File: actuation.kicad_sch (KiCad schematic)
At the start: 16 parts, among them J1 ACTUATION, U1 PCA9615

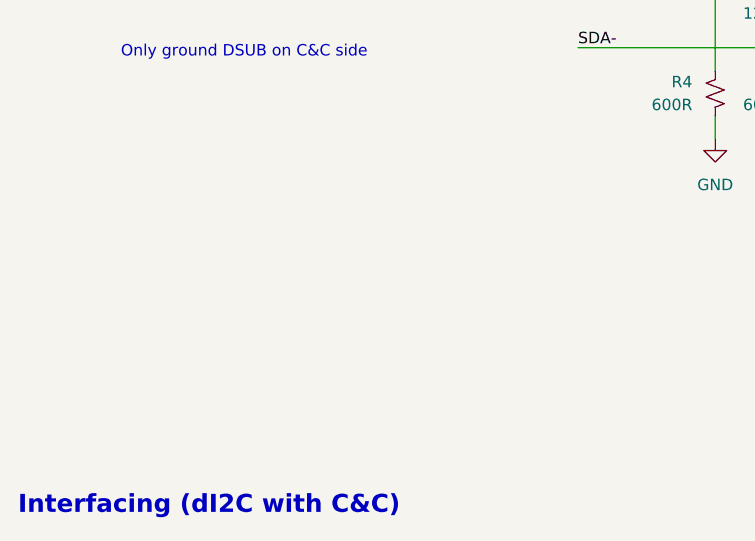
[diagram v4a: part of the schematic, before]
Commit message: TVS diodes for ESD protection on inputs
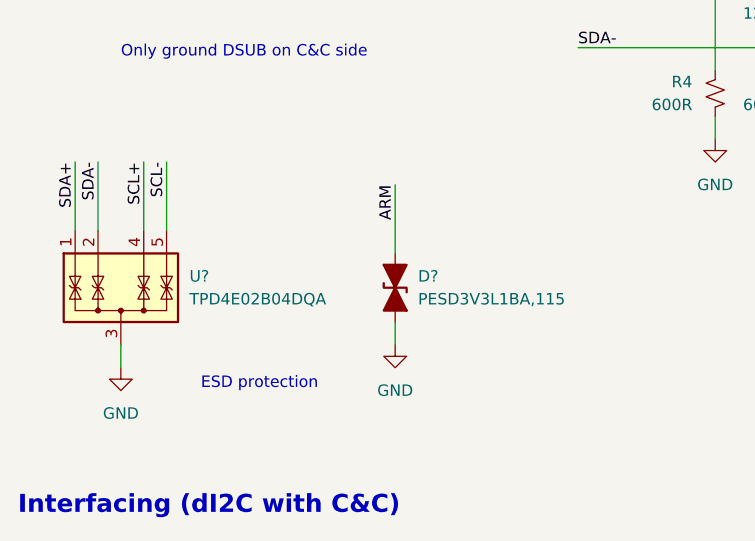
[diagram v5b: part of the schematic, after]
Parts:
- added D?: PESD3V3L1BA,115, Diode_SMD:D_SOD-323, symbol Device:D_TVS_Filled
- added U?: TPD4E02B04DQA, Package_SON:USON-10_2.5x1.0mm_P0.5mm, symbol Power_Protection:TPD4E02B04DQA
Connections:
- net ARM: now also D?.2 (A2)
- net GND: now also D?.1 (A1), U?.3 (G), U?.8 (G)
- net SCL+: now also U?.4 (IO3)
- net SCL-: now also U?.5 (IO4)
- net SDA+: now also U?.1 (IO1)
- net SDA-: now also U?.2 (IO2)
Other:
- note added: "ESD protection"
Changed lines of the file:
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@@
+    (stroke (width 0) (type default) (color 0 0 0 0))
+  )
+  (wire (pts (xy 58.42 96.52) (xy 58.42 104.14))
     (stroke (width 0) (type default) (color 0 0 0 0))
   )
@@
     (stroke (width 0) (type default) (color 0 0 0 0))
   )
+  (wire (pts (xy 25.4 93.98) (xy 25.4 101.6))
+    (stroke (width 0) (type default) (color 0 0 0 0))
+  )
   (wire (pts (xy 143.51 41.91) (xy 143.51 39.37))
     (stroke (width 0) (type default) (color 0 0 0 0))
@@
     (stroke (width 0) (type default) (color 0 0 0 0))
   )
+  (wire (pts (xy 58.42 111.76) (xy 58.42 114.3))
+    (stroke (width 0) (type default) (color 0 0 0 0))
+  )
   (wire (pts (xy 40.64 52.07) (xy 33.02 52.07))
     (stroke (width 0) (type default) (color 0 0 0 0))
@@
     (stroke (width 0) (type default) (color 0 0 0 0))
   )
+  (wire (pts (xy 22.86 93.98) (xy 22.86 101.6))
+    (stroke (width 0) (type default) (color 0 0 0 0))
+  )
   (wire (pts (xy 218.44 81.28) (xy 224.79 81.28))
     (stroke (width 0) (type default) (color 0 0 0 0))
@@
     (stroke (width 0) (type default) (color 0 0 0 0))
   )
+  (wire (pts (xy 30.48 93.98) (xy 30.48 101.6))
+    (stroke (width 0) (type default) (color 0 0 0 0))
+  )
   (wire (pts (xy 143.51 29.21) (xy 143.51 31.75))
     (stroke (width 0) (type default) (color 0 0 0 0))
@@
     (stroke (width 0) (type default) (color 0 0 0 0))
   )
+  (wire (pts (xy 27.94 114.3) (xy 27.94 116.84))
+    (stroke (width 0) (type default) (color 0 0 0 0))
+  )
   (wire (pts (xy 114.3 57.15) (xy 114.3 54.61))
     (stroke (width 0) (type default) (color 0 0 0 0))
@@
   )
   (wire (pts (xy 35.56 44.45) (xy 43.18 44.45))
+    (stroke (width 0) (type default) (color 0 0 0 0))
+  )
+  (wire (pts (xy 33.02 93.98) (xy 33.02 101.6))
     (stroke (width 0) (type default) (color 0 0 0 0))
   )
@@
     (effects (font (size 1.27 1.27)) (justify left bottom))
   )
+  (text "ESD protection" (at 36.83 119.38 0)
+    (effects (font (size 1.27 1.27)) (justify left bottom))
+  )
   (text "~33mA 3.3V consumption" (at 222.25 44.45 0)
     (effects (font (size 1.27 1.27)) (justify left bottom))
@@
     (effects (font (size 1.27 1.27)) (justify left bottom))
   )
+  (label "SCL+" (at 30.48 93.98 270)
+    (effects (font (size 1.27 1.27)) (justify right bottom))
+  )
+  (label "SDA+" (at 22.86 93.98 270)
+    (effects (font (size 1.27 1.27)) (justify right bottom))
+  )
+  (label "ARM" (at 58.42 96.52 270)
+    (effects (font (size 1.27 1.27)) (justify right bottom))
+  )
   (label "SCL-" (at 78.74 66.04 0)
     (effects (font (size 1.27 1.27)) (justify left bottom))
@@
   (label "SDA-" (at 35.56 46.99 0)
     (effects (font (size 1.27 1.27)) (justify left bottom))
+  )
+  (label "SDA-" (at 25.4 93.98 270)
+    (effects (font (size 1.27 1.27)) (justify right bottom))
+  )
+  (label "SCL-" (at 33.02 93.98 270)
+    (effects (font (size 1.27 1.27)) (justify right bottom))
   )
   (label "SDA" (at 168.91 69.85 180)
@@
     )
     (property "Datasheet" "" (id 3) (at 33.02 69.85 0)
+      (effects (font (size 1.27 1.27)) hide)
+    )
+    (pin "1")
+  )
+  (symbol (lib_name "GND_1") (lib_id "power:GND") (at 58.42 114.3 0) (unit 1)
+    (in_bom yes) (on_board yes) (fields_autoplaced)
+    (property "Reference" "#PWR?" (id 0) (at 58.42 120.65 0)
+      (effects (font (size 1.27 1.27)) hide)
+    )
+    (property "Value" "GND" (id 1) (at 58.42 119.38 0))
+    (property "Footprint" "" (id 2) (at 58.42 114.3 0)
+      (effects (font (size 1.27 1.27)) hide)
+    )
+    (property "Datasheet" "" (id 3) (at 58.42 114.3 0)
       (effects (font (size 1.27 1.27)) hide)
     )
@@
     (pin "1")
   )
+  (symbol (lib_id "Power_Protection:TPD4E02B04DQA") (at 27.94 109.22 0) (unit 1)
+    (in_bom yes) (on_board yes) (fields_autoplaced)
+    (property "Reference" "U?" (id 0) (at 35.56 106.6799 0)
+      (effects (font (size 1.27 1.27)) (justify left))
+    )
+    (property "Value" "TPD4E02B04DQA" (id 1) (at 35.56 109.2199 0)
+      (effects (font (size 1.27 1.27)) (justify left))
+    )
+    (property "Footprint" "Package_SON:USON-10_2.5x1.0mm_P0.5mm" (id 2) (at 35.56 109.22 0)
+      (effects (font (size 1.27 1.27)) (justify left) hide)
+    )
+    (property "Datasheet" "http://www.ti.com/lit/ds/symlink/tpd4e02b04.pdf" (id 3) (at 31.115 100.965 0)
+      (effects (font (size 1.27 1.27)) hide)
+    )
+    (property "MPN" "TPD4E02B04DQAR" (id 4) (at 27.94 109.22 0)
+      (effects (font (size 1.27 1.27)) hide)
+    )
+    (pin "3")
+    (pin "1")
+    (pin "10")
+    (pin "2")
+    (pin "4")
+    (pin "5")
+    (pin "6")
+    (pin "7")
+    (pin "8")
+    (pin "9")
+  )
   (symbol (lib_id "power:GND") (at 93.98 91.44 0) (mirror y) (unit 1)
     (in_bom yes) (on_board yes) (fields_autoplaced)
@@
     )
     (property "Datasheet" "" (id 3) (at 104.14 45.72 0)
+      (effects (font (size 1.27 1.27)) hide)
+    )
+    (pin "1")
+  )
+  (symbol (lib_name "GND_1") (lib_id "power:GND") (at 27.94 116.84 0) (unit 1)
+    (in_bom yes) (on_board yes) (fields_autoplaced)
+    (property "Reference" "#PWR?" (id 0) (at 27.94 123.19 0)
+      (effects (font (size 1.27 1.27)) hide)
+    )
+    (property "Value" "GND" (id 1) (at 27.94 121.92 0))
+    (property "Footprint" "" (id 2) (at 27.94 116.84 0)
+      (effects (font (size 1.27 1.27)) hide)
+    )
+    (property "Datasheet" "" (id 3) (at 27.94 116.84 0)
       (effects (font (size 1.27 1.27)) hide)
     )
@@
     (pin "2")
   )
+  (symbol (lib_id "Device:D_TVS_Filled") (at 58.42 107.95 90) (unit 1)
+    (in_bom yes) (on_board yes) (fields_autoplaced)
+    (property "Reference" "D?" (id 0) (at 60.96 106.6799 90)
+      (effects (font (size 1.27 1.27)) (justify right))
+    )
+    (property "Value" "PESD3V3L1BA,115" (id 1) (at 60.96 109.2199 90)
+      (effects (font (size 1.27 1.27)) (justify right))
+    )
+    (property "Footprint" "Diode_SMD:D_SOD-323" (id 2) (at 58.42 107.95 0)
+      (effects (font (size 1.27 1.27)) hide)
+    )
+    (property "Datasheet" "~" (id 3) (at 58.42 107.95 0)
+      (effects (font (size 1.27 1.27)) hide)
+    )
+    (property "MPN" "PESD3V3L1BA,115" (id 4) (at 58.42 107.95 90)
+      (effects (font (size 1.27 1.27)) hide)
+    )
+    (pin "1")
+    (pin "2")
+  )
   (symbol (lib_id "Device:R_Small_US") (at 153.67 62.23 0) (mirror y) (unit 1)
     (in_bom yes) (on_board yes)
@@
       (reference "#PWR?") (unit 1) (value "GND") (footprint "")
     )
+    (path "/1b3e1420-3438-499c-8f85-e9b1856ceae6"
+      (reference "#PWR?") (unit 1) (value "GND") (footprint "")
+    )
     (path "/6d7df23a-0810-4327-8a09-0091cb17fdd4/2130f65f-0e67-469a-972e-96733d3b3a2f"
       (reference "#PWR?") (unit 1) (value "+3.3V") (footprint "")
@@
       (reference "#PWR?") (unit 1) (value "VBUS") (footprint "")
     )
+    (path "/b57e0df7-51bf-49fb-a99b-7a6872f6ad20"
+      (reference "#PWR?") (unit 1) (value "GND") (footprint "")
+    )
     (path "/6d7df23a-0810-4327-8a09-0091cb17fdd4/b9dc7b7c-9fa1-4f3b-8ff8-0ba754a0b762"
       (reference "#PWR?") (unit 1) (value "GNDPWR") (footprint "")
@@
       (reference "D?") (unit 1) (value "FB PWR") (footprint "LED_SMD:LED_0603_1608Metric")
     )
+    (path "/e8f74dd7-19c8-4b0c-ad93-af053471099d"
+      (reference "D?") (unit 1) (value "PESD3V3L1BA,115") (footprint "Diode_SMD:D_SOD-323")
+    )
     (path "/73a2f7f3-4823-454a-bfba-81a74cbf18fe"
       (reference "J1") (unit 1) (value "ACTUATION") (footprint "actuation:182-009-213R561")
@@
       (reference "U?") (unit 1) (value "LP5912-3.3DRV") (footprint "Package_SON:WSON-6-1EP_2x2mm_P0.65mm_EP1x1.6mm_ThermalVias")
     )
+    (path "/9b0439aa-b796-4ae0-a275-c210befba1ed"
+      (reference "U?") (unit 1) (value "TPD4E02B04DQA") (footprint "Package_SON:USON-10_2.5x1.0mm_P0.5mm")
+    )
     (path "/6d7df23a-0810-4327-8a09-0091cb17fdd4/af114d4a-a977-4217-bb94-36d026f527c7"

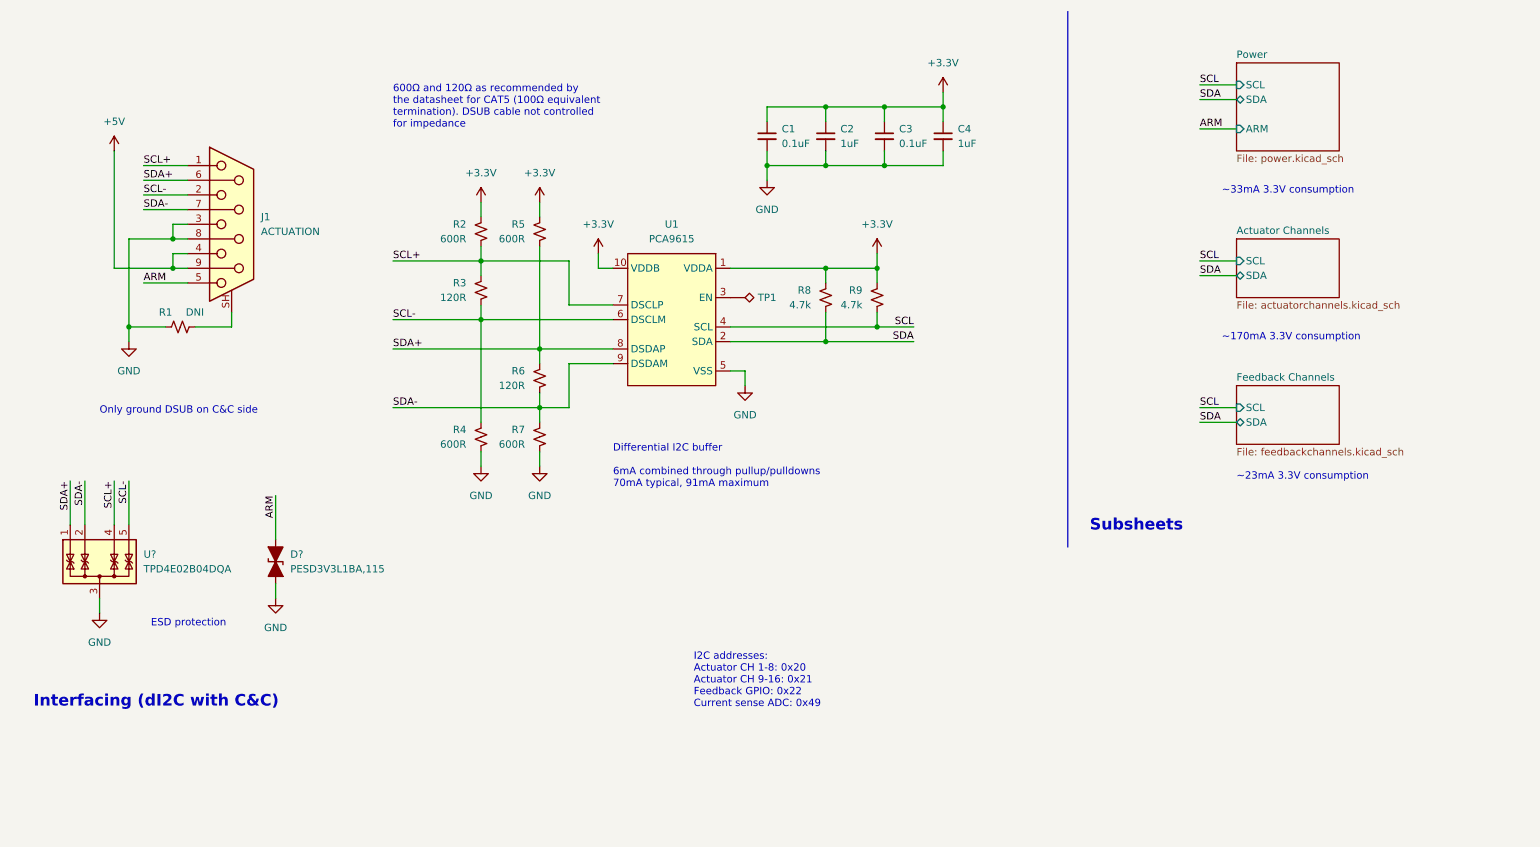
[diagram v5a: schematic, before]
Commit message: Added power protection as well
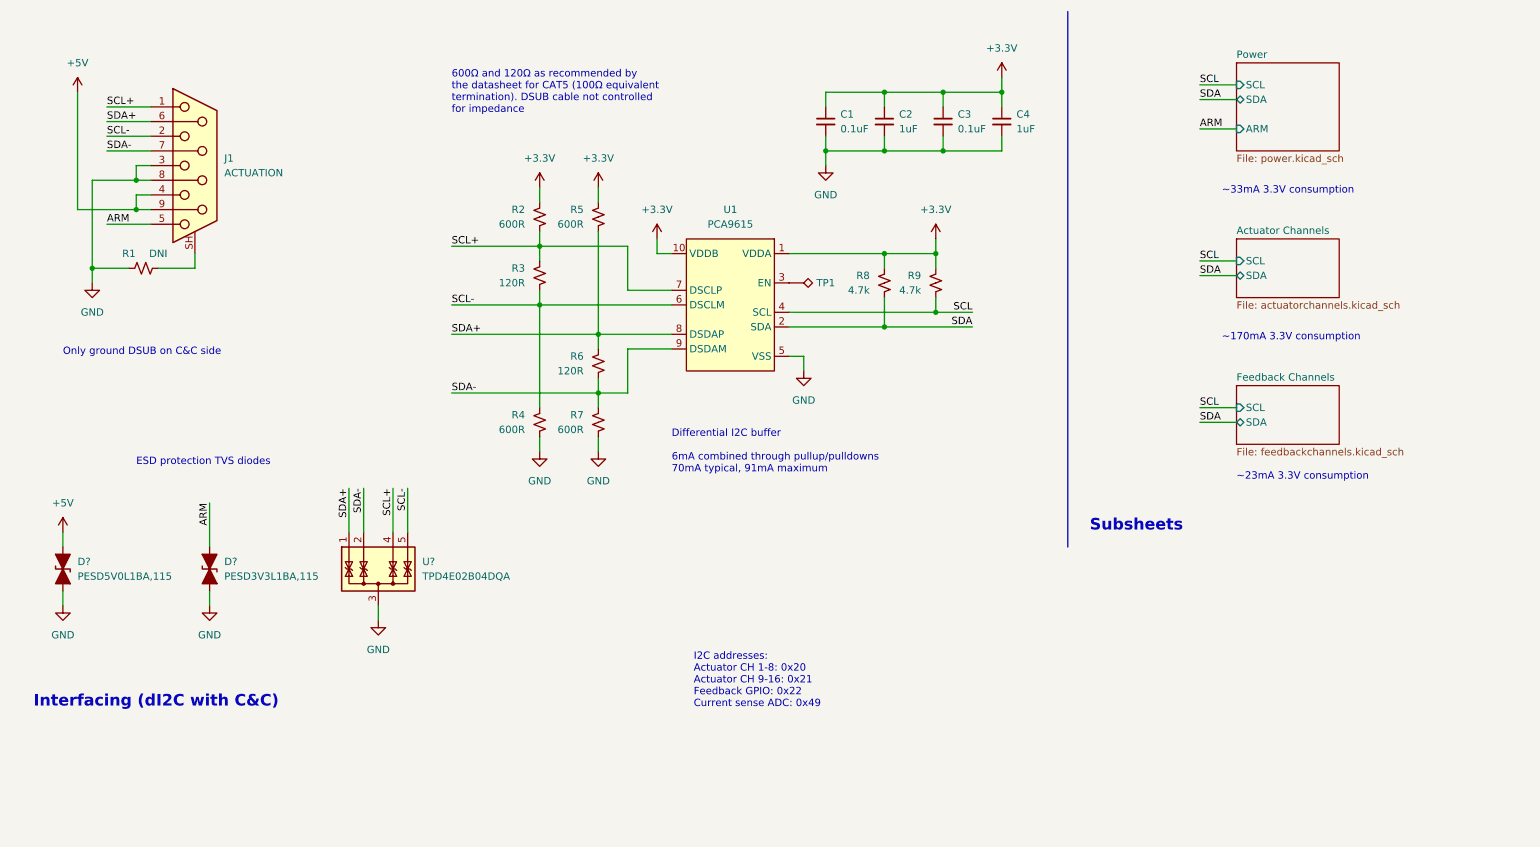
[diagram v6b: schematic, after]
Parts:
- added D?: PESD5V0L1BA,115, Diode_SMD:D_SOD-323, symbol Device:D_TVS_Filled
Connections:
- net +5V: now also D?.2 (A2)
- net GND: now also D?.1 (A1)
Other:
- note added: "ESD protection TVS diodes"
- note removed: "ESD protection"
- moved on the sheet: C1, C2, C3, C4, D?, J1, R1, R2, R3, R4, R5, R6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
